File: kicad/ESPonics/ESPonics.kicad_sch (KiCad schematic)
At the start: 5 parts, among them J1 RJ45, J2 RJ45, J3 RJ45, J4 Conn_01x02_Pin, U1 ESP32-DevKitC

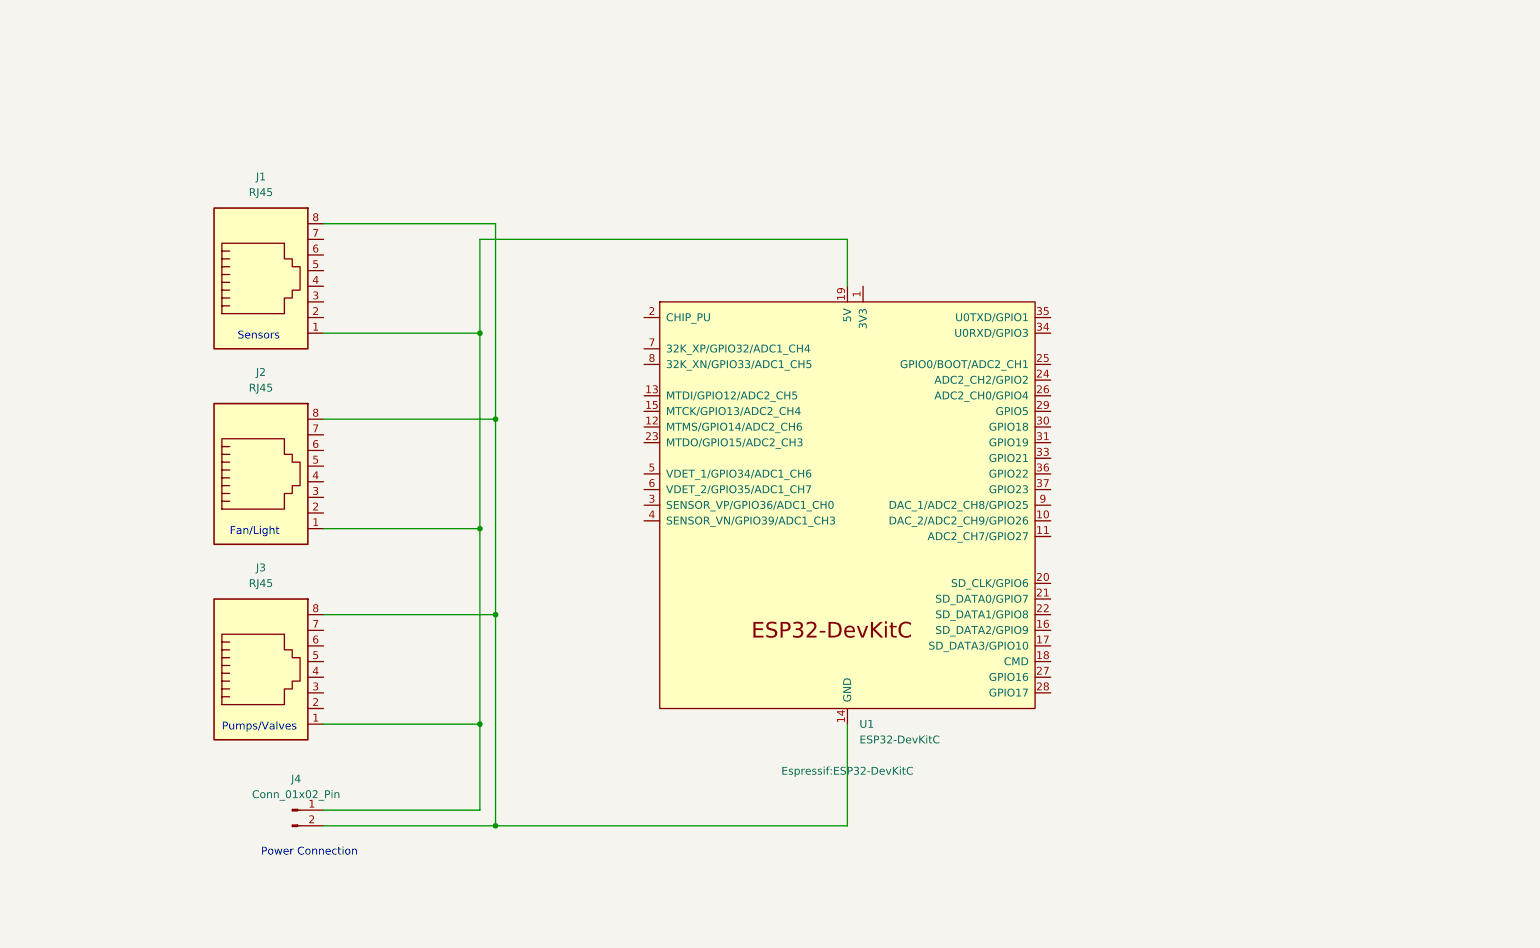
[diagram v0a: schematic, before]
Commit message: Add GPIO connections to kicad
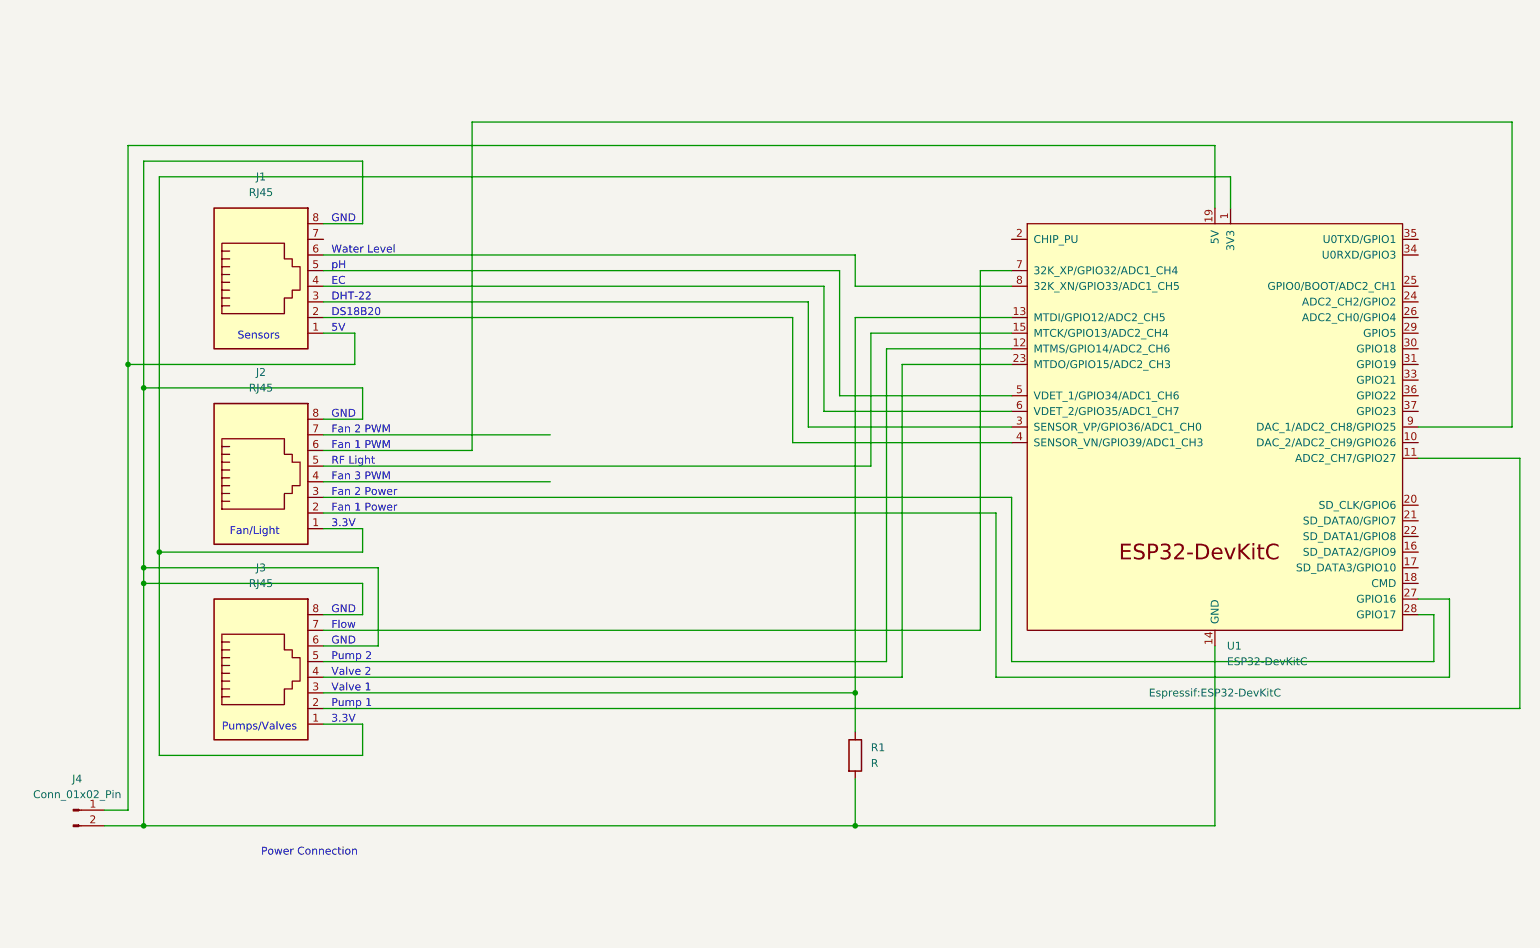
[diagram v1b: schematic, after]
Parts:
- added R1: R, symbol Device:R
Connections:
- net at J1.1, J4.1 (Pin_1), U1.19 (5V): no longer J2.1, J3.1
- net at J3.2: now also U1.11 (ADC2_CH7/GPIO27)
- net at J3.3: now also U1.13 (MTDI/GPIO12/ADC2_CH5), R1.1
- net at J3.4: now also U1.23 (MTDO/GPIO15/ADC2_CH3)
- net at J3.5: now also U1.12 (MTMS/GPIO14/ADC2_CH6)
- net at J3.6: now also J1.8, J2.8, J3.8, J4.2 (Pin_2), U1.14 (GND), U1.32 (GND), U1.38 (GND), R1.2
- net at J3.7: now also U1.7 (32K_XP/GPIO32/ADC1_CH4)
- net at J2.2: now also U1.27 (GPIO16)
- net at J2.3: now also U1.28 (GPIO17)
- net at J2.5: now also U1.15 (MTCK/GPIO13/ADC2_CH4)
- net at J2.6: now also U1.9 (DAC_1/ADC2_CH8/GPIO25)
- net at U1.1 (3V3): now also J2.1, J3.1
- net at U1.3 (SENSOR_VP/GPIO36/ADC1_CH0): now also J1.3
- net at U1.4 (SENSOR_VN/GPIO39/ADC1_CH3): now also J1.2
- net at U1.5 (VDET_1/GPIO34/ADC1_CH6): now also J1.5
- net at U1.6 (VDET_2/GPIO35/ADC1_CH7): now also J1.4
- net at U1.8 (32K_XN/GPIO33/ADC1_CH5): now also J1.6
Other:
- note added: "3.3V"
- note added: "5V"
- note added: "DHT-22"
- note added: "DS18B20"
- note added: "EC"
- note added: "Fan 1 PWM"
- note added: "Fan 1 Power"
- note added: "Fan 2 PWM"
- note added: "Fan 2 Power"
- note added: "Fan 3 PWM"
- note added: "Flow"
- note added: "GND"
- note added: "Pump 1"
- note added: "Pump 2"
- note added: "RF Light"
- note added: "Valve 1"
- note added: "Valve 2"
- note added: "Water Level"
- note added: "pH"
- moved on the sheet: J4, U1

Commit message: Add pull up resistors
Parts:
- added R2, R3: R, symbol Device:R
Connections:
- net at J2.1, J3.1, U1.1 (3V3): now also R2.1, R3.1
- net at J1.3, U1.3 (SENSOR_VP/GPIO36/ADC1_CH0): now also R3.2
- net at J1.2, U1.4 (SENSOR_VN/GPIO39/ADC1_CH3): now also R2.2
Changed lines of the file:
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@@
   (junction (at 35.56 151.13) (diameter 0) (color 0 0 0 0)
   )
+  (junction (at 101.6 45.72) (diameter 0) (color 0 0 0 0)
+  )
+  (junction (at 93.98 45.72) (diameter 0) (color 0 0 0 0)
+  )
+  (junction (at 93.98 68.58) (diameter 0) (color 0 0 0 0)
+  )
   (junction (at 38.1 106.68) (diameter 0) (color 0 0 0 0)
   )
@@
   (junction (at 151.13 129.54) (diameter 0) (color 0 0 0 0)
   )
+  (junction (at 101.6 66.04) (diameter 0) (color 0 0 0 0)
+  )
   (junction (at 151.13 151.13) (diameter 0) (color 0 0 0 0)
   )
-  (wire (pts (xy 64.77 68.58) (xy 140.97 68.58))
+  (wire (pts (xy 64.77 68.58) (xy 93.98 68.58))
     (stroke (width 0) (type default))
   )
@@
     (stroke (width 0) (type default))
   )
+  (wire (pts (xy 93.98 45.72) (xy 93.98 49.53))
+    (stroke (width 0) (type default))
+  )
   (wire (pts (xy 64.77 63.5) (xy 146.05 63.5))
     (stroke (width 0) (type default))
@@
     (stroke (width 0) (type default))
   )
+  (wire (pts (xy 93.98 57.15) (xy 93.98 68.58))
+    (stroke (width 0) (type default))
+  )
+  (wire (pts (xy 101.6 45.72) (xy 93.98 45.72))
+    (stroke (width 0) (type default))
+  )
   (wire (pts (xy 257.81 86.36) (xy 257.81 36.83))
     (stroke (width 0) (type default))
@@
     (stroke (width 0) (type default))
   )
+  (wire (pts (xy 101.6 45.72) (xy 101.6 49.53))
+    (stroke (width 0) (type default))
+  )
+  (wire (pts (xy 101.6 57.15) (xy 101.6 66.04))
+    (stroke (width 0) (type default))
+  )
   (wire (pts (xy 38.1 139.7) (xy 71.12 139.7))
     (stroke (width 0) (type default))
@@
     (stroke (width 0) (type default))
   )
+  (wire (pts (xy 93.98 45.72) (xy 38.1 45.72))
+    (stroke (width 0) (type default))
+  )
   (wire (pts (xy 247.65 127) (xy 247.65 114.3))
     (stroke (width 0) (type default))
@@
     (stroke (width 0) (type default))
   )
+  (wire (pts (xy 101.6 66.04) (xy 143.51 66.04))
+    (stroke (width 0) (type default))
+  )
   (wire (pts (xy 35.56 80.01) (xy 71.12 80.01))
     (stroke (width 0) (type default))
@@
     (stroke (width 0) (type default))
   )
+  (wire (pts (xy 93.98 68.58) (xy 140.97 68.58))
+    (stroke (width 0) (type default))
+  )
   (wire (pts (xy 35.56 151.13) (xy 151.13 151.13))
     (stroke (width 0) (type default))
@@
     (stroke (width 0) (type default))
   )
-  (wire (pts (xy 64.77 66.04) (xy 143.51 66.04))
+  (wire (pts (xy 64.77 66.04) (xy 101.6 66.04))
     (stroke (width 0) (type default))
   )
@@
     (stroke (width 0) (type default))
   )
-  (wire (pts (xy 212.09 45.72) (xy 38.1 45.72))
+  (wire (pts (xy 212.09 45.72) (xy 101.6 45.72))
     (stroke (width 0) (type default))
   )
@@
   (text "Pumps/Valves" (at 48.26 135.89 0)
     (effects (font (size 1.27 1.27)) (justify left bottom))
+  )
+  (symbol (lib_id "Device:R") (at 101.6 53.34 0) (unit 1)
+    (in_bom yes) (on_board yes) (dnp no) (fields_autoplaced)
+    (property "Reference" "R3" (at 104.14 52.07 0)
+      (effects (font (size 1.27 1.27)) (justify left))
+    )
+    (property "Value" "R" (at 104.14 54.61 0)
+      (effects (font (size 1.27 1.27)) (justify left))
+    )
+    (property "Footprint" "" (at 99.822 53.34 90)
+      (effects (font (size 1.27 1.27)) hide)
+    )
+    (property "Datasheet" "~" (at 101.6 53.34 0)
+      (effects (font (size 1.27 1.27)) hide)
+    )
+    (pin "1")
+    (pin "2")
+    (instances
+      (project "ESPonics"
+        (path "/c3daf4c9-5e4c-4393-8644-666075c44fa8"
+          (reference "R3") (unit 1)
+        )
+      )
+    )
   )
   (symbol (lib_id "Connector:RJ45") (at 54.61 127 0) (unit 1)
@@
         )
       )
+    )
+  )
+  (symbol (lib_id "Device:R") (at 93.98 53.34 0) (unit 1)
+    (in_bom yes) (on_board yes) (dnp no) (fields_autoplaced)
+    (property "Reference" "R2" (at 96.52 52.07 0)
+      (effects (font (size 1.27 1.27)) (justify left))
+    )
+    (property "Value" "R" (at 96.52 54.61 0)
+      (effects (font (size 1.27 1.27)) (justify left))
+    )
+    (property "Footprint" "" (at 92.202 53.34 90)
+      (effects (font (size 1.27 1.27)) hide)
+    )
+    (property "Datasheet" "~" (at 93.98 53.34 0)
+      (effects (font (size 1.27 1.27)) hide)
+    )
+    (pin "1")
+    (pin "2")
+    (instances
+      (project "ESPonics"
+        (path "/c3daf4c9-5e4c-4393-8644-666075c44fa8"
+          (reference "R2") (unit 1)
+        )
+      )

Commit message: Start creating first pcb
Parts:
- R1: value R -> 47k
- R2: value R -> 4.7k; footprint (none) -> Resistor_THT:R_Axial_DIN0204_L3.6mm_D1.6mm_P1.90mm_Vertical
- R3: value R -> 10k; footprint (none) -> Resistor_THT:R_Axial_DIN0204_L3.6mm_D1.6mm_P1.90mm_Vertical
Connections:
- net GND: now reaches J1.8, J2.8, J3.6, J3.8, J4.2 (Pin_2), R1.2, U1.14 (GND), U1.32 (GND), U1.38 (GND)
- net +5V: now reaches J1.1, J4.1 (Pin_1), U1.19 (5V)
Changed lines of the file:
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@@
   (junction (at 38.1 106.68) (diameter 0) (color 0 0 0 0)
   )
+  (junction (at 212.09 48.26) (diameter 0) (color 0 0 0 0)
+  )
   (junction (at 35.56 111.76) (diameter 0) (color 0 0 0 0)
   )
   (junction (at 151.13 129.54) (diameter 0) (color 0 0 0 0)
   )
+  (junction (at 29.21 148.59) (diameter 0) (color 0 0 0 0)
+  )
   (junction (at 101.6 66.04) (diameter 0) (color 0 0 0 0)
   )
+  (junction (at 29.21 26.67) (diameter 0) (color 0 0 0 0)
+  )
+  (junction (at 29.21 158.75) (diameter 0) (color 0 0 0 0)
+  )
+  (junction (at 29.21 151.13) (diameter 0) (color 0 0 0 0)
+  )
   (junction (at 151.13 151.13) (diameter 0) (color 0 0 0 0)
   )
@@
     (stroke (width 0) (type default))
   )
-  (wire (pts (xy 212.09 45.72) (xy 212.09 50.8))
+  (wire (pts (xy 212.09 45.72) (xy 212.09 48.26))
     (stroke (width 0) (type default))
   )
@@
     (stroke (width 0) (type default))
   )
+  (wire (pts (xy 29.21 26.67) (xy 29.21 148.59))
+    (stroke (width 0) (type default))
+  )
   (wire (pts (xy 242.57 86.36) (xy 257.81 86.36))
     (stroke (width 0) (type default))
@@
     (stroke (width 0) (type default))
   )
+  (wire (pts (xy 212.09 48.26) (xy 212.09 50.8))
+    (stroke (width 0) (type default))
+  )
   (wire (pts (xy 151.13 143.51) (xy 151.13 151.13))
     (stroke (width 0) (type default))
@@
     (stroke (width 0) (type default))
   )
+  (wire (pts (xy 29.21 25.4) (xy 29.21 26.67))
+    (stroke (width 0) (type default))
+  )
   (wire (pts (xy 64.77 66.04) (xy 101.6 66.04))
     (stroke (width 0) (type default))
@@
     (stroke (width 0) (type default))
   )
+  (wire (pts (xy 29.21 151.13) (xy 29.21 158.75))
+    (stroke (width 0) (type default))
+  )
+  (wire (pts (xy 29.21 158.75) (xy 29.21 162.56))
+    (stroke (width 0) (type default))
+  )
   (wire (pts (xy 73.66 109.22) (xy 73.66 121.92))
     (stroke (width 0) (type default))
@@
       (effects (font (size 1.27 1.27)) (justify left))
     )
-    (property "Value" "R" (at 104.14 54.61 0)
-      (effects (font (size 1.27 1.27)) (justify left))
-    )
-    (property "Footprint" "" (at 99.822 53.34 90)
+    (property "Value" "10k" (at 104.14 54.61 0)
+      (effects (font (size 1.27 1.27)) (justify left))
+    )
+    (property "Footprint" "Resistor_THT:R_Axial_DIN0204_L3.6mm_D1.6mm_P1.90mm_Vertical" (at 99.822 53.34 90)
       (effects (font (size 1.27 1.27)) hide)
     )
@@
         (path "/c3daf4c9-5e4c-4393-8644-666075c44fa8"
           (reference "R3") (unit 1)
+        )
+      )
+    )
+  )
+  (symbol (lib_id "power:GND") (at 29.21 162.56 0) (unit 1)
+    (in_bom yes) (on_board yes) (dnp no) (fields_autoplaced)
+    (property "Reference" "#PWR01" (at 29.21 168.91 0)
+      (effects (font (size 1.27 1.27)) hide)
+    )
+    (property "Value" "GND" (at 29.21 167.64 0)
+      (effects (font (size 1.27 1.27)))
+    )
+    (property "Footprint" "" (at 29.21 162.56 0)
+      (effects (font (size 1.27 1.27)) hide)
+    )
+    (property "Datasheet" "" (at 29.21 162.56 0)
+      (effects (font (size 1.27 1.27)) hide)
+    )
+    (pin "1")
+    (instances
+      (project "ESPonics"
+        (path "/c3daf4c9-5e4c-4393-8644-666075c44fa8"
+          (reference "#PWR01") (unit 1)
         )
       )
@@
       (effects (font (size 1.27 1.27)) (justify left))
     )
-    (property "Value" "R" (at 96.52 54.61 0)
-      (effects (font (size 1.27 1.27)) (justify left))
-    )
-    (property "Footprint" "" (at 92.202 53.34 90)
+    (property "Value" "4.7k" (at 96.52 54.61 0)
+      (effects (font (size 1.27 1.27)) (justify left))
+    )
+    (property "Footprint" "Resistor_THT:R_Axial_DIN0204_L3.6mm_D1.6mm_P1.90mm_Vertical" (at 92.202 53.34 90)
       (effects (font (size 1.27 1.27)) hide)
     )
@@
         (path "/c3daf4c9-5e4c-4393-8644-666075c44fa8"
           (reference "R2") (unit 1)
+        )
+      )
+    )
+  )
+  (symbol (lib_id "power:PWR_FLAG") (at 29.21 26.67 90) (unit 1)
+    (in_bom yes) (on_board yes) (dnp no) (fields_autoplaced)
+    (property "Reference" "#FLG02" (at 27.305 26.67 0)
+      (effects (font (size 1.27 1.27)) hide)
+    )
+    (property "Value" "PWR_FLAG" (at 25.4 26.67 90)
+      (effects (font (size 1.27 1.27)) (justify left))
+    )
+    (property "Footprint" "" (at 29.21 26.67 0)
+      (effects (font (size 1.27 1.27)) hide)
+    )
+    (property "Datasheet" "~" (at 29.21 26.67 0)
+      (effects (font (size 1.27 1.27)) hide)
+    )
+    (pin "1")
+    (instances
+      (project "ESPonics"
+        (path "/c3daf4c9-5e4c-4393-8644-666075c44fa8"
+          (reference "#FLG02") (unit 1)
         )
       )
@@
     )
   )
+  (symbol (lib_id "power:PWR_FLAG") (at 29.21 158.75 90) (unit 1)
+    (in_bom yes) (on_board yes) (dnp no) (fields_autoplaced)
+    (property "Reference" "#FLG01" (at 27.305 158.75 0)
+      (effects (font (size 1.27 1.27)) hide)
+    )
+    (property "Value" "PWR_FLAG" (at 25.4 158.75 90)
+      (effects (font (size 1.27 1.27)) (justify left))
+    )
+    (property "Footprint" "" (at 29.21 158.75 0)
+      (effects (font (size 1.27 1.27)) hide)
+    )
+    (property "Datasheet" "~" (at 29.21 158.75 0)
+      (effects (font (size 1.27 1.27)) hide)
+    )
+    (pin "1")
+    (instances
+      (project "ESPonics"
+        (path "/c3daf4c9-5e4c-4393-8644-666075c44fa8"
+          (reference "#FLG01") (unit 1)
+        )
+      )
+    )
+  )
   (symbol (lib_id "Device:R") (at 151.13 139.7 0) (unit 1)
     (in_bom yes) (on_board yes) (dnp no) (fields_autoplaced)
@@
       (effects (font (size 1.27 1.27)) (justify left))
     )
-    (property "Value" "R" (at 153.67 140.97 0)
+    (property "Value" "47k" (at 153.67 140.97 0)
       (effects (font (size 1.27 1.27)) (justify left))
     )
@@
         )
       )
+    )
+  )
+  (symbol (lib_id "power:PWR_FLAG") (at 212.09 48.26 270) (mirror x) (unit 1)
+    (in_bom yes) (on_board yes) (dnp no)
+    (property "Reference" "#FLG03" (at 213.995 48.26 0)
+      (effects (font (size 1.27 1.27)) hide)
+    )
+    (property "Value" "PWR_FLAG" (at 215.9 48.26 90)
+      (effects (font (size 1.27 1.27)) (justify left))
+    )
+    (property "Footprint" "" (at 212.09 48.26 0)
+      (effects (font (size 1.27 1.27)) hide)
+    )
+    (property "Datasheet" "~" (at 212.09 48.26 0)
+      (effects (font (size 1.27 1.27)) hide)
+    )
+    (pin "1")
+    (instances
+      (project "ESPonics"
+        (path "/c3daf4c9-5e4c-4393-8644-666075c44fa8"
+          (reference "#FLG03") (unit 1)
+        )
+      )
+    )
+  )
+  (symbol (lib_id "power:+5V") (at 29.21 25.4 0) (unit 1)
+    (in_bom yes) (on_board yes) (dnp no) (fields_autoplaced)
+    (property "Reference" "#PWR02" (at 29.21 29.21 0)
+      (effects (font (size 1.27 1.27)) hide)
+    )
+    (property "Value" "+5V" (at 29.21 20.32 0)
+      (effects (font (size 1.27 1.27)))
+    )
+    (property "Footprint" "" (at 29.21 25.4 0)
+      (effects (font (size 1.27 1.27)) hide)
+    )
+    (property "Datasheet" "" (at 29.21 25.4 0)
+      (effects (font (size 1.27 1.27)) hide)
+    )
+    (pin "1")
+    (instances
+      (project "ESPonics"
+        (path "/c3daf4c9-5e4c-4393-8644-666075c44fa8"
+          (reference "#PWR02") (unit 1)
+        )
+      )
